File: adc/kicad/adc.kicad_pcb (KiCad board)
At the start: 2 copper layers, 90 x 88.4 mm, 114 parts, among them J1 Conn_01x07_Pin, J2 Conn_01x02_Pin, J3 Conn_01x02_Pin, J4 Conn_01x02_Pin, J5 pcie_98, U1 ADS1261BIRHBT, U2 ESD5344D-TP, U3 TPS7A2050PDBVR, U4 TPS7A2025PDBVRr, U6 TPS65135, U7 ADP7182AUJZ-5.0, U8 ADP7182AUJZ-2.5, U9 XC6206P332MR

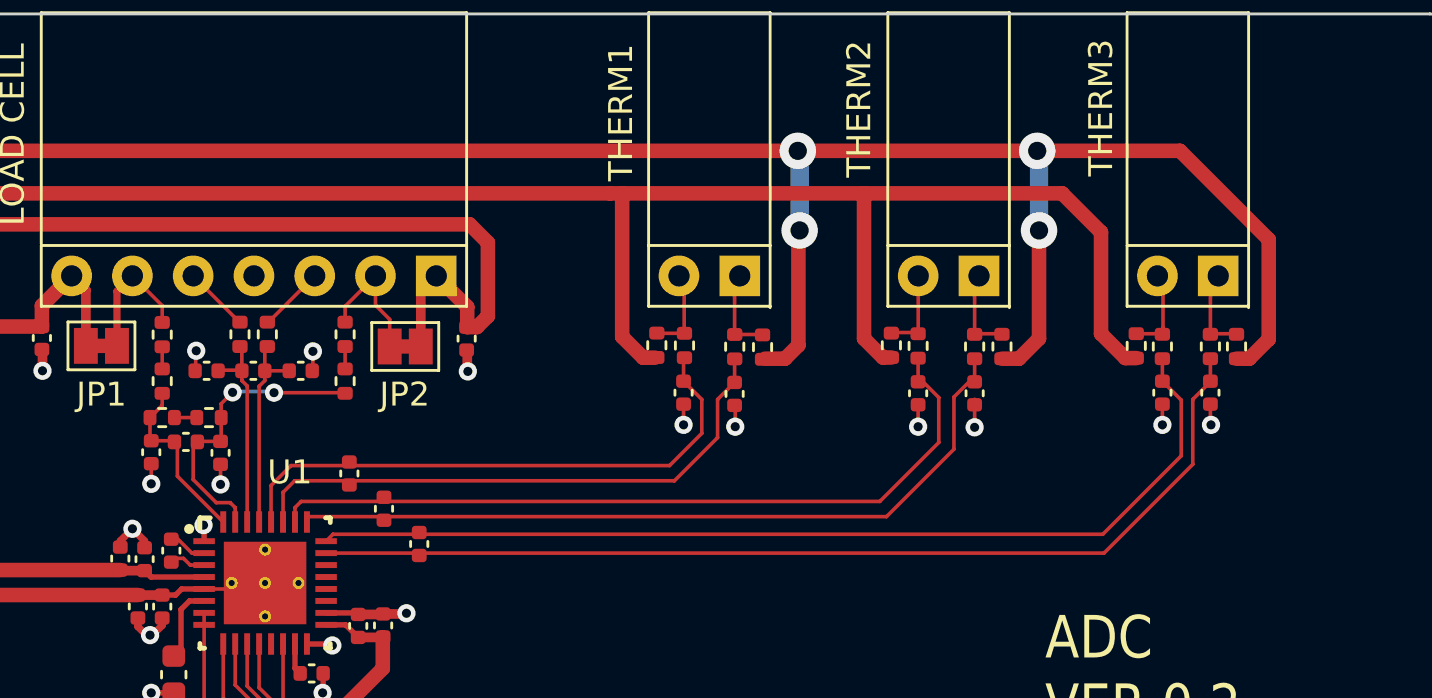
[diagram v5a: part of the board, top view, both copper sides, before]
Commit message: Updated the thermistor inputs to use 2K voltage divider.
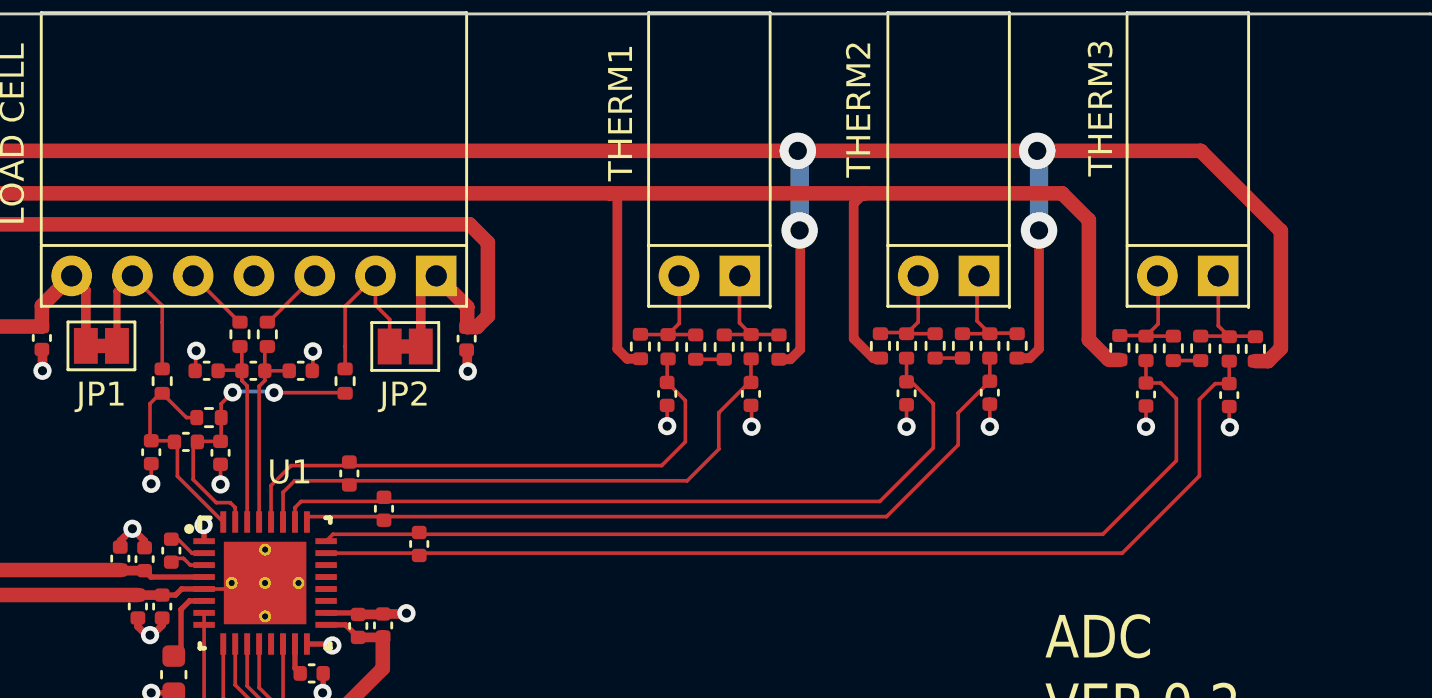
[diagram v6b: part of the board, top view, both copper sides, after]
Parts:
- removed R14, R17, R35: 1K 0.1% 10ppm, Resistor_SMD:R_0402_1005Metric
- added R37: 2K 0.1%, Resistor_SMD:R_0402_1005Metric, F.Cu at (29.2, -74.5)
- added R38: 2K 0.1%, Resistor_SMD:R_0402_1005Metric, F.Cu at (30.4, -74.5)
- added R39: 2K 0.1%, Resistor_SMD:R_0402_1005Metric, F.Cu at (39.2, -74.5)
- added R40: 2K 0.1%, Resistor_SMD:R_0402_1005Metric, F.Cu at (40.3, -74.5)
- added R41: 2K 0.1%, Resistor_SMD:R_0402_1005Metric, F.Cu at (49.1, -74.4)
- added R42: 2K 0.1%, Resistor_SMD:R_0402_1005Metric, F.Cu at (50.3, -74.4)
- R1, R12, R13, R2, R3, R30, R36, R7, R8: value 1K 0.1% 10ppm -> 2K 0.1%
- moved C8 0.79 mm to (51.5, -72.5)
- moved R11 0.79 mm to (51.5, -74.4)
- moved R8 0.79 mm to (52.6, -74.4)
- moved C7 0.69 mm to (48.0, -72.5)
- moved R10 0.69 mm to (48.0, -74.4)
- moved R7 0.69 mm to (46.9, -74.4)
- moved C3 0.69 mm to (28.0, -72.5)
- moved R3 0.69 mm to (26.8, -74.5)
- moved R6 0.69 mm to (28.0, -74.5)
- moved R12 0.69 mm to (32.6, -74.5)
- moved C9 0.69 mm to (31.5, -72.5)
- moved R9 0.69 mm to (31.5, -74.5)
- moved C4 0.64 mm to (41.5, -72.6)
- moved R5 0.64 mm to (41.5, -74.5)
- moved R2 0.64 mm to (42.6, -74.5)
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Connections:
- R13 pad 2: Net-(R13-Pad2) -> Net-(J1-Pin_6)
- R30 pad 2: Net-(R14-Pad1) -> /AIN0
- R36 pad 2: Net-(R35-Pad1) -> Net-(J1-Pin_2)
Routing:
- net Net-(J1-Pin_2): track 5.65 -> 7.61 mm
- net Net-(J1-Pin_6): track 5.65 -> 7.60 mm
- net /AIN0: track 7.40 -> 9.31 mm
- net Net-(J3-Pin_1): track 3.41 -> 4.93 mm
- net Net-(J3-Pin_2): track 3.45 -> 4.94 mm
- net Net-(J4-Pin_2): track 3.24 -> 4.60 mm
- net Net-(R37-Pad1): track 0.00 -> 1.19 mm
- net Net-(R39-Pad1): track 0.00 -> 1.14 mm
- net Net-(R41-Pad1): track 0.00 -> 1.14 mm
- net Net-(J2-Pin_1): track 3.84 -> 4.93 mm
- net Net-(J4-Pin_1): track 3.67 -> 4.75 mm
- net /AIN9: track 42.5 -> 43.5 mm
- net Net-(R35-Pad1): track 0.94 -> 0.00 mm
- net Net-(R14-Pad1): track 0.94 -> 0.00 mm
- net Net-(J2-Pin_2): track 3.69 -> 4.62 mm
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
